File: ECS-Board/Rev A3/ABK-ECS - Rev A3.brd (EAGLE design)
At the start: 100 x 80 mm, 245 parts, among them J10 22-05-7068-06, J11 FTSH-105-01-L-DV-NOPASTE, J2 USB-B-S-RA, J21 FTSH-103-01-L-DV-NOPASTE, J4 MSTBA2, J5 22-05-7068-06, J6 22-05-7028-02, J7 22-05-7068-06, J8 22-05-7068-06, J9 22-05-7028-02, K1 G6K-2G-Y, SW1 B3FS-1015, SW2 B3FS-1015, T1 EXMACHINA-LOGO-NAME, T10 MMBT2222AL, T11 MMBT2222AL, T12 IRLML5103TRPBF, T13 IRLML5103TRPBF, T14 IRLML5103TRPBF, T15 IRLML5103TRPBF, T16 MMBT2222AL, T17 MMBT2222AL, T18 MMBT2222AL, T19 MMBT2222AL, T2 IRLML5103TRPBF, T3 MMBT2222AL, T4 IRLML5103TRPBF, T5 IRLML5103TRPBF, T6 IRLML5103TRPBF, T7 IRLML5103TRPBF, T8 MMBT2222AL, T9 MMBT2222AL, U1 AT24C512C-SSHM-B, U2 LPC1768FBD100, U3 LT3686HDDPBF, U4 LT3686HDDPBF, U6 CD4050BD, U7 CD4050BD, X1 FC-135, X2 ASE-12, X3 3000

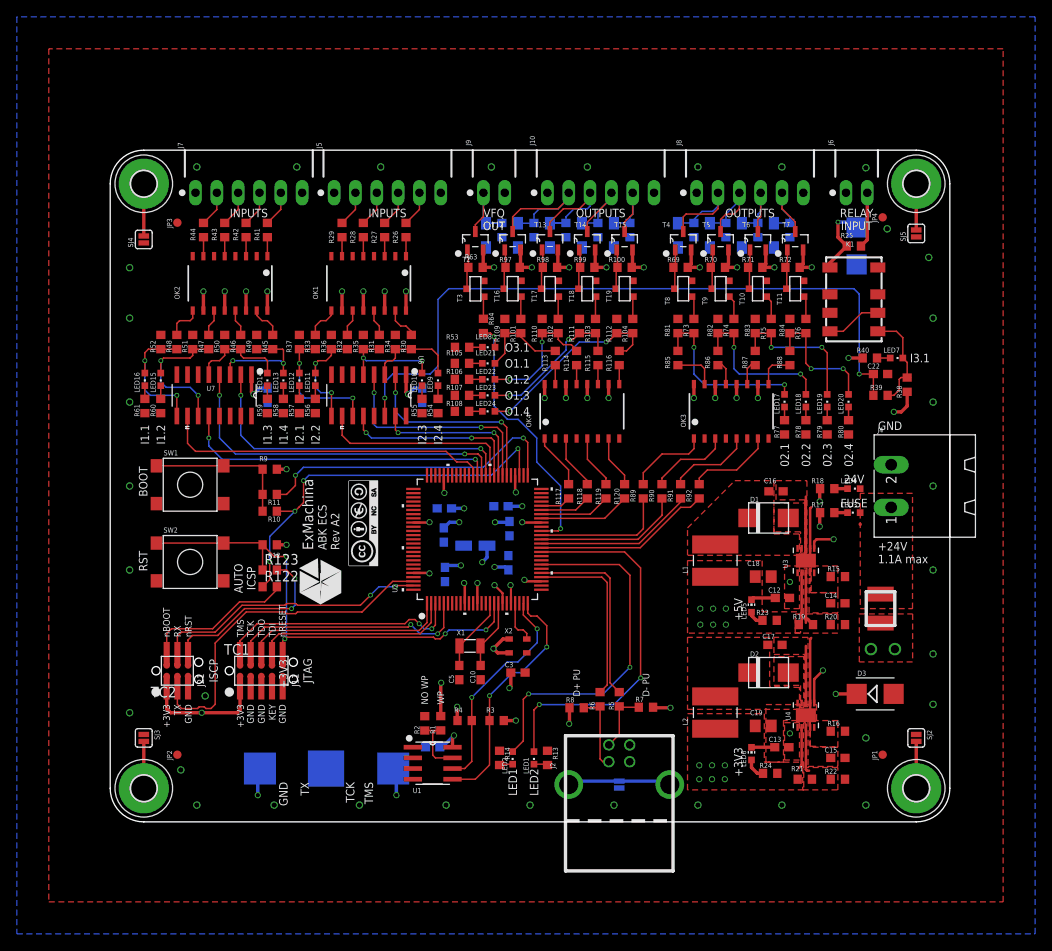
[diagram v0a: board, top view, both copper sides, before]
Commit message: Propagate changes from Rev A2a to Rev A3
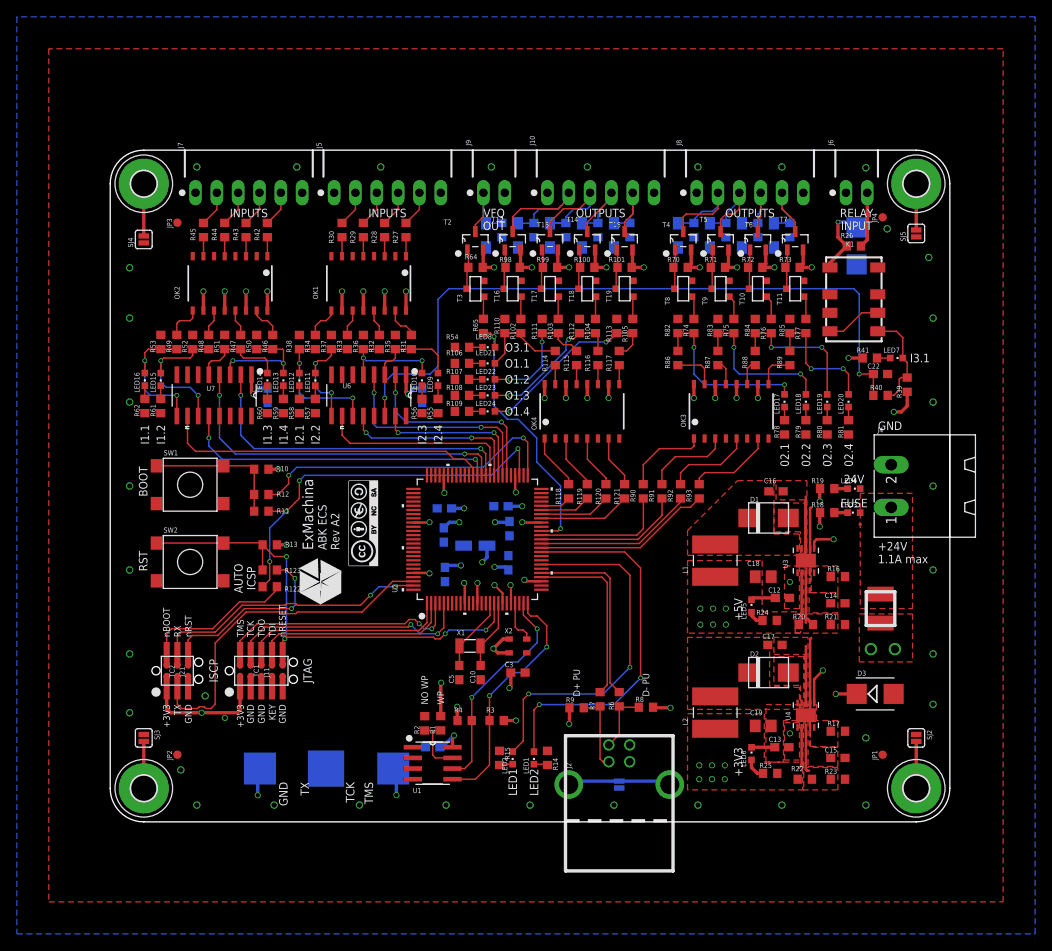
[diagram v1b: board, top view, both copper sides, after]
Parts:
- removed R5: 33, rcl:R0603
- added R121: 330, rcl:R0603
- LED21: value 01.1 -> Blue
- LED5, LED6: device led:CHIP-LED0603 -> led:CHIPLED_0603
- R1: value 4K7 -> 4K7, DNI
- R10: value 0R -> 10K
- R100, R63, R69, R70, R71, R72, R97, R98, R99: value 330 -> 10K
- R101, R64, R73: value 100 -> 10K
- R102, R103, R104, R74, R75, R76: value 100 -> 1K
- R105, R77: value 1K5 -> 1K
- R109, R81: value 4K7 -> 1K5
- R113, R85: value 1K -> 4K7
- R114, R115, R116, R26, R86, R87, R88: value 1K -> 100
- R117, R89: value 330 -> 100
- R12: value 10K -> 0R
- R13, R23: value 1K5 -> 10K
- R15: value 31K6 -> 1K5
- R17: value 4K7 -> 31K6
- R19: value 52K3 -> 4K7
- R20: value 10K -> 52K3
- R21: value 31K6 -> 10K
- R22: value 10K -> 31K6
- R25: value 100 -> 1K5
- R34, R49: value 4K7 -> 1K
- R39: value 100 -> 4K7
- R40: value 1K5 -> 100
- R41: value 1K -> 1K5
- R53: value 1K5 -> 4K7
- R62: value 10K -> 1K5
- R65: value 10K -> 100
- R7: value 1K5 -> 33
- R8: value 1K5 -> 1K5, DNI
- R9: value 10K -> 1K5, DNI
- R93: value 10K -> 330
- moved R41 73.4 mm to (90.5, 55.2), turned to 180 degrees
- moved R38 72.6 mm to (22.5, 57.1)
- moved R25 63.6 mm to (78.6, 5.78), turned to 0 degrees
- moved R26 53.4 mm to (88.6, 68.6), turned to 180 degrees
- moved R62 47.4 mm to (4.13, 49.5), flipped to the top, turned to 270 degrees
- moved R9 46.3 mm to (55.5, 13.6)
- moved R15 45.7 mm to (46.4, 7.62), turned to 90 degrees
- moved R13 41.7 mm to (19.0, 33.0), turned to 0 degrees
- moved R93 36.8 mm to (70.2, 39.4), flipped to the top, turned to 270 degrees
- moved R53 35.9 mm to (6.03, 57.1), turned to 90 degrees
- moved R65 27.5 mm to (44.5, 59.1), flipped to the top, turned to 270 degrees
- moved R17 26.1 mm to (86.7, 10.8)
- moved R81 23.6 mm to (87.9, 47.0), turned to 270 degrees
- moved R89 23.6 mm to (81.0, 55.2)
- moved R105 20.8 mm to (62.2, 59.1), turned to 90 degrees
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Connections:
- net !RESET: now also R13.1; no longer R12.1
- net +24V: now also R101.2, R19.2, R64.2, R73.2; no longer R17.2, R63.2, R69.2, R97.2
- net +3V3: now also R10.2, R13.2, R22.2, R25.2, R9.1; no longer R12.2, R21.2, R24.2, R7.1, R9.2
- net +5V: now also R20.2, R24.2, R39.1, R41.2; no longer R19.2, R23.2, R38.1, R40.2
- net BOOT_SELECT_P2_10: now also R11.1; no longer R10.1
- net BOOT_SELECT_P2_12: now also R12.1; no longer R11.1
- net GND: now also R113.2, R15.2, R17.1, R21.1, R23.1, R38.2, R62.2, R63.1, R69.1, R85.2, R97.1; no longer R105.2, R13.2, R15.1, R20.1, R22.1, R34.2, R49.2, R62.1, R65.1, R77.2, R93.1
- net INPUT1.1: now also R49.2, R53.1; no longer R48.2, R52.1
- net INPUT1.2: now also R48.2, R52.1; no longer R47.2, R51.1
- net INPUT1.3: now also R47.2, R51.1; no longer R46.2, R50.1
- net INPUT1.4: now also R46.2, R50.1; no longer R45.2, R49.1
- net INPUT2.1: now also R34.2, R38.1; no longer R33.2, R37.1
- net INPUT2.2: now also R33.2, R37.1; no longer R32.2, R36.1
- net INPUT2.3: now also R32.2, R36.1; no longer R31.2, R35.1
- net INPUT2.4: now also R31.2, R35.1; no longer R30.2, R34.1
- net INPUT3.1: now also R40.2; no longer R39.2
- net MOTOR_VFQ: now also R63.2; no longer R62.2
- net N$1: now also R7.1, R9.2; no longer R6.1, R8.2
- net N$100: now also R46.1; no longer R45.1
- net N$101: now also R43.2; no longer R42.2
- net N$102: now also R43.1; no longer R42.1
- net N$103: now also R47.1; no longer R46.1
- net N$104: now also R44.2; no longer R43.2
- net N$105: now also R44.1; no longer R43.1
- net N$106: now also R48.1; no longer R47.1
- net N$107: now also R59.1; no longer R58.1
- net N$108: now also R60.1; no longer R59.1
- net N$109: now also R61.1; no longer R60.1
- net N$110: now also R49.1; no longer R48.1
- net N$111: now also R45.2; no longer R44.2
- net N$112: now also R45.1; no longer R44.1
- net N$13: now also R22.1, R23.2; no longer R21.1, R22.2
- net N$17: now also R74.2; no longer R73.2
- net N$18: now also R70.1; no longer R69.1
- net N$19: now also R75.2; no longer R74.2
- net N$2: now also R6.1, R8.2; no longer R5.1, R7.2
- net N$20: now also R71.1; no longer R70.1
- net N$21: now also R76.2; no longer R75.2
- net N$22: now also R72.1; no longer R71.1
- net N$23: now also R77.2; no longer R76.2
- net N$24: now also R73.1; no longer R72.1
- net N$25: now also R65.1; no longer R64.1
- net N$26: now also R64.1; no longer R63.1
- net N$28: now also R26.2; no longer R25.2
- net N$29: now also R14.1; no longer R13.1
- net N$3: now also R15.1; no longer R14.1
- net N$31: now also R102.1, R110.1, R114.1; no longer R101.1, R109.1, R113.1
- net N$32: now also R26.1; no longer R25.1
- net N$33: now also R114.2; no longer R113.2
- net N$34: now also R103.1, R111.1, R115.1; no longer R102.1, R110.1, R114.1
- net N$35: now also R115.2; no longer R114.2
- net N$36: now also R104.1, R112.1, R116.1; no longer R103.1, R111.1, R115.1
- net N$37: now also R105.1, R113.1, R117.1; no longer R104.1, R112.1, R116.1
- net N$38: now also R116.2; no longer R115.2
- net N$39: now also R117.2; no longer R116.2
- net N$4: now also R16.2; no longer R15.2
- net N$40: now also R118.1; no longer R117.1
- net N$41: now also R27.2; no longer R26.2
- net N$42: now also R119.1; no longer R118.1
- net N$43: now also R121.1; no longer R120.1
- net N$44: now also R19.1; no longer R18.1
- net N$45: now also R18.1; no longer R17.1
- net N$46: now also R120.1; no longer R119.1
- net N$47: now also R28.2; no longer R27.2
- net N$48: now also R29.2; no longer R28.2
- net N$49: now also R30.2; no longer R29.2
- net N$5: now also R10.1, R12.2; no longer R10.2, R9.1
- net N$50: now also R25.1; no longer R24.1
- net N$51: now also R24.1; no longer R23.1
- net N$52: now also R30.1; no longer R29.1
- net N$53: now also R29.1; no longer R28.1
- net N$54: now also R28.1; no longer R27.1
- net N$55: now also R27.1; no longer R26.1
- net N$56: now also R54.1; no longer R53.1
- net N$57: now also R55.1; no longer R54.1
- net N$58: now also R56.1; no longer R55.1
- net N$59: now also R57.1; no longer R56.1
- net N$61: now also R34.1; no longer R33.1
- net N$62: now also R33.1; no longer R32.1
- net N$63: now also R32.1; no longer R31.1
- net N$64: now also R31.1; no longer R30.1
- net N$65: now also R58.1; no longer R57.1
- net N$66: now also R106.1; no longer R105.1
- net N$67: now also R107.1; no longer R106.1
- net N$68: now also R108.1; no longer R107.1
- net N$69: now also R109.1; no longer R108.1
- net N$7: now also R17.2; no longer R16.2
- net N$71: now also R98.1; no longer R97.1
- net N$72: now also R99.1; no longer R98.1
- net N$73: now also R39.2, R40.1; no longer R38.2, R39.1
- net N$74: now also R41.1; no longer R40.1
- net N$75: now also R74.1, R82.1, R86.1; no longer R73.1, R81.1, R85.1
- net N$76: now also R86.2; no longer R85.2
- net N$77: now also R100.1; no longer R99.1
- net N$78: now also R101.1; no longer R100.1
- net N$79: now also R75.1, R83.1, R87.1; no longer R74.1, R82.1, R86.1
- net N$80: now also R87.2; no longer R86.2
- net N$81: now also R42.2; no longer R41.2
- net N$82: now also R42.1; no longer R41.1
- net N$83: now also R76.1, R84.1, R88.1; no longer R75.1, R83.1, R87.1
- net N$84: now also R102.2; no longer R101.2
- net N$85: now also R103.2; no longer R102.2
- net N$86: now also R77.1, R85.1, R89.1; no longer R76.1, R84.1, R88.1
- net N$87: now also R88.2; no longer R87.2
- net N$88: now also R89.2; no longer R88.2
- net N$89: now also R90.1; no longer R89.1
- net N$9: now also R20.1, R21.2; no longer R19.1, R20.2
- net N$90: now also R62.1; no longer R61.1
- net N$91: now also R91.1; no longer R90.1
- net N$92: now also R93.1; no longer R92.1
- net N$93: now also R92.1; no longer R91.1
- net N$94: now also R78.1; no longer R77.1
- net N$95: now also R79.1; no longer R78.1
- net N$96: now also R80.1; no longer R79.1
- net N$97: now also R81.1; no longer R80.1
- net N$98: now also R104.2; no longer R103.2
- net N$99: now also R105.2; no longer R104.2
- net OUTPUT1.1: now also R94.2; no longer R93.2
- net OUTPUT1.1_MCU: now also R118.2; no longer R117.2
- net OUTPUT1.2: now also R95.2; no longer R94.2
- net OUTPUT1.2_MCU: now also R119.2; no longer R118.2
- net OUTPUT1.3: now also R96.2; no longer R95.2
- net OUTPUT1.3_MCU: now also R120.2; no longer R119.2
- net OUTPUT1.4: now also R97.2; no longer R96.2
- net OUTPUT1.4_MCU: now also R121.2; no longer R120.2
- net OUTPUT2.1: now also R66.2; no longer R65.2
- net OUTPUT2.1_MCU: now also R90.2; no longer R89.2
- net OUTPUT2.2: now also R67.2; no longer R66.2
- net OUTPUT2.2_MCU: now also R91.2; no longer R90.2
- net OUTPUT2.3: now also R68.2; no longer R67.2
- net OUTPUT2.3_MCU: now also R92.2; no longer R91.2
- net OUTPUT2.4: now also R69.2; no longer R68.2
- net OUTPUT2.4_MCU: now also R93.2; no longer R92.2
- net OUTPUT3.2_MCU: now also R65.2; no longer R64.2
- net USB_D_N: now also R6.2; no longer R5.2
- net USB_D_P: now also R7.2; no longer R6.2
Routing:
- net N$5: track 17.8 -> 16.8 mm
- net BOOT_SELECT_P2_12: track 37.6 -> 38.4 mm
- net N$91: track 9.75 -> 10.3 mm
- net GND: vias 34 -> 36
